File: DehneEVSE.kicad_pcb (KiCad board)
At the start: 2 copper layers, 188 x 98 mm, 57 parts, among them J1 Connector1, J3 FC68131, J4 FC68131, J5 FC68131, K1 G5NB-1A Relay 5VDC, Q1 PN2222A, T1 VB_05-1-12, T2 VB_05-1-12, T3 VB_05-1-12, U1 Arduino Nano 33 IoT, U2 IRM-05-5, U3 LT1498IN8#PBF, U4 mcp6291-e_p-nd, U5 mcp6291-e_p-nd, U6 mcp6291-e_p-nd

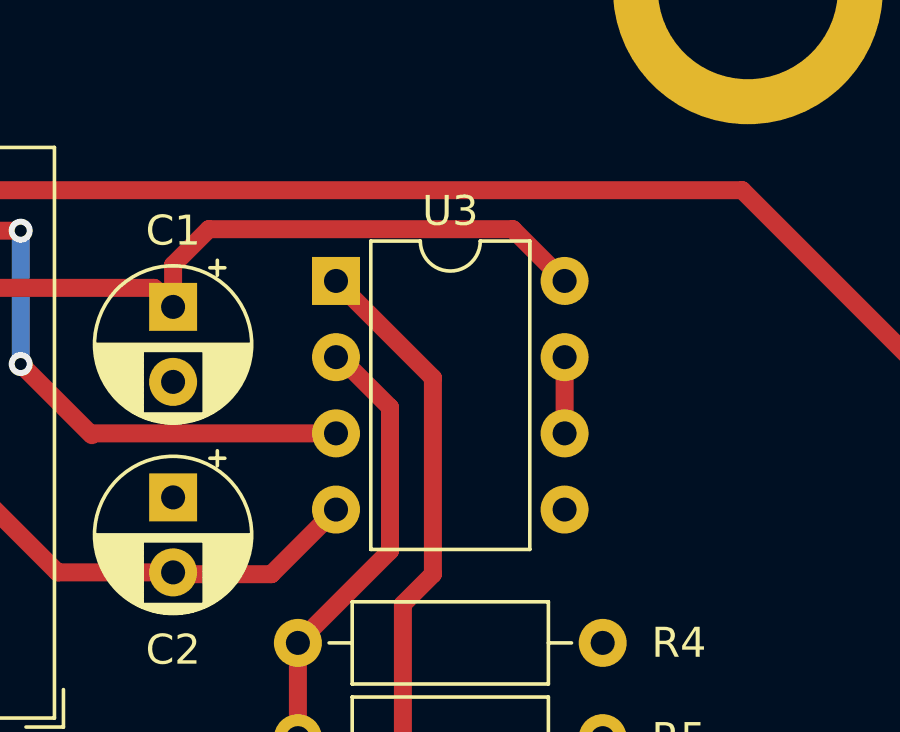
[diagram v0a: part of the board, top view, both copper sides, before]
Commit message: renamed to DehneEVSE
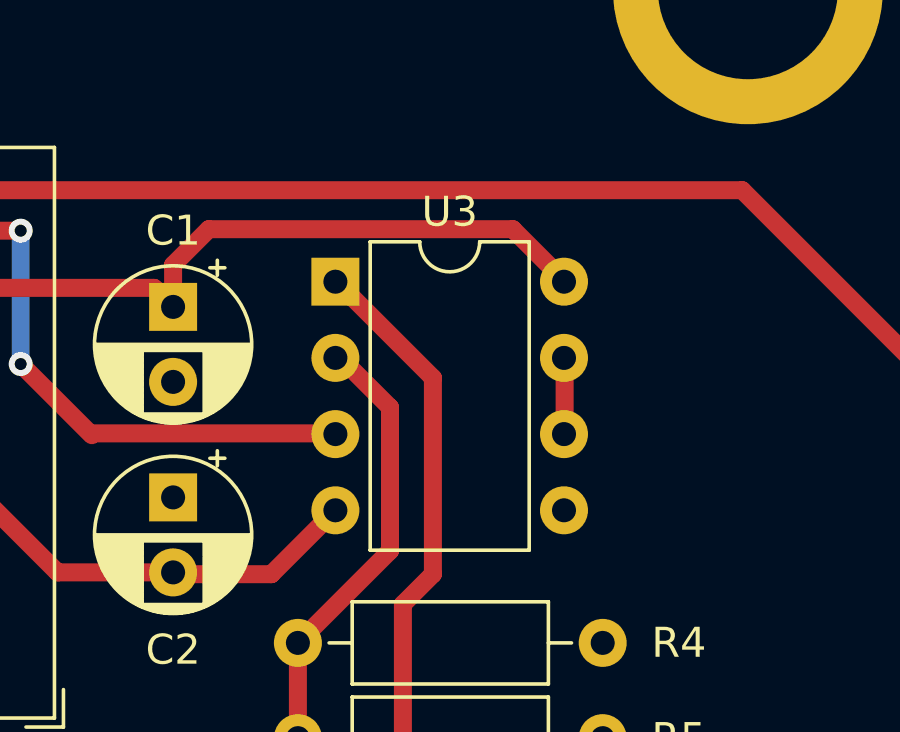
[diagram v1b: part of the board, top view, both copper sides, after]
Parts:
- J1: footprint EVChargingStation:conn_08x02_wago -> DehneEVSEFootPrints:conn_08x02_wago
- J3, J4, J5: footprint EVChargingStation:CLIFF_FC68131 -> DehneEVSEFootPrints:CLIFF_FC68131
- K1: footprint EVChargingStation:Omron-GSNB-1A -> DehneEVSEFootPrints:Omron-GSNB-1A
- REF** (x9): footprint EVChargingStation:MountingHole_6mm -> DehneEVSEFootPrints:MountingHole_6mm
- T1, T2, T3: footprint EVChargingStation:VB_05-1-12 -> DehneEVSEFootPrints:VB_05-1-12
- U1: footprint EVChargingStation:Arduino Nano - THT -> DehneEVSEFootPrints:Arduino Nano - THT
- U2: footprint EVChargingStation:CONV_IRM-05-5 -> DehneEVSEFootPrints:CONV_IRM-05-5
- U3: value LT1498IN8#PBF -> LT1498IN8
